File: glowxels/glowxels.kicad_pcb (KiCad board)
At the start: 2 copper layers, 97.3 x 25 mm, 83 parts, among them J1 OUT, J2 IN, U1 STP16CPC26, U2 STP16CPC26, U3 STP16CPC26, U4 STP16CPC26

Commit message: Silkscreen optimization: mark power rails on back.
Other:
- board text added: "GND"
- board text added: "V-LED"
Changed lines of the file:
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@@
   (general
     (thickness 1.6)
-    (drawings 30)
+    (drawings 32)
     (tracks 581)
     (zones 0)
@@
   )
   (setup
-    (last_trace_width 0.3)
+    (last_trace_width 0.18)
     (user_trace_width 0.2)
     (user_trace_width 0.25)
@@
     (descr "Through hole straight pin header, 1x05, 1.27mm pitch, single row")
     (tags "Through hole pin header THT 1x05 1.27mm single row")
-    (fp_text reference J2 (at 0 -1.695 180) (layer F.SilkS)
+    (fp_text reference J2 (at 1.439 -2.085 180) (layer F.SilkS)
       (effects (font (size 1 1) (thickness 0.15)))
     )
@@
     (descr "Through hole straight pin header, 1x05, 1.27mm pitch, single row")
     (tags "Through hole pin header THT 1x05 1.27mm single row")
-    (fp_text reference J1 (at 0 -1.695 180) (layer F.SilkS)
+    (fp_text reference J1 (at -1.046 -2.085 180) (layer F.SilkS)
       (effects (font (size 1 1) (thickness 0.15)))
     )
@@
     )
   )
+  (gr_text V-LED (at 180.649 95.22) (layer B.SilkS)
+    (effects (font (size 1.5 1.5) (thickness 0.3)) (justify mirror))
+  )
+  (gr_text GND (at 180.849 104.32) (layer B.SilkS)
+    (effects (font (size 1.5 1.5) (thickness 0.3)) (justify mirror))
+  )
   (gr_arc (start 193.4 111.5) (end 193.4 112.5) (angle -90) (layer Edge.Cuts) (width 0.1))

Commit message: Add OSHW silkscreen.
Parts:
- added REF***: OSHW-Symbol_6.7x6mm_SilkScreen, Symbols:OSHW-Symbol_6.7x6mm_SilkScreen, F.Cu at (147.2, 90.3)
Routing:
- net /LED-Power: track 0.00 -> 167.7 mm
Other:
- board text added: "M2.5"

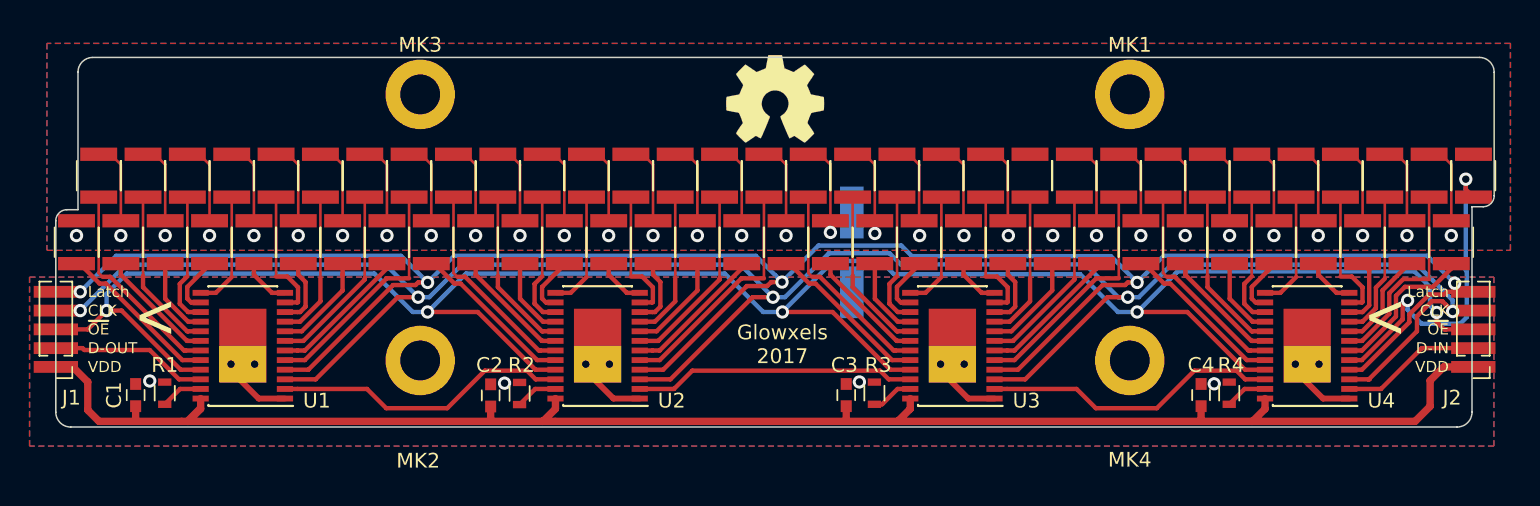
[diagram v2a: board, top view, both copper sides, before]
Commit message: Chaining connector: use space and increase pitch 1.27mm -> 2.0mm
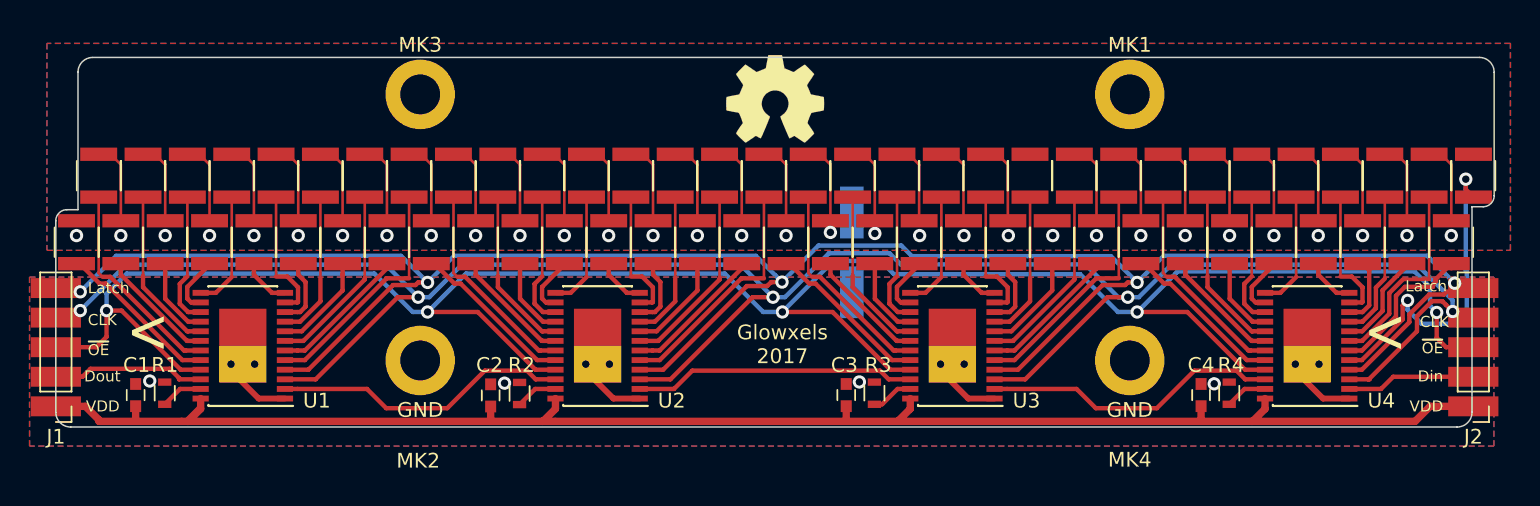
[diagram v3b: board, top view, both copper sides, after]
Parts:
- J1, J2: footprint Pin_Headers:Pin_Header_Straight_1x05_Pitch1.27mm -> Pin_Headers:Pin_Header_Straight_1x05_Pitch2.00mm
- moved J1 2.67 mm to (98.6, 111.1)
- moved J2 2.67 mm to (194.5, 111.1)
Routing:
- net /~OE: track 146.9 -> 151.4 mm
- net /VDD: track 115.2 -> 110.9 mm
- net /D-IN: track 9.53 -> 8.73 mm
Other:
- board text added: "Din"
- board text added: "Dout"
- board text removed: "D-IN"
- board text removed: "D-OUT"
